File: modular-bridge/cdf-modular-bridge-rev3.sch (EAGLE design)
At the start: 25 parts, among them Q1 Ixgh48n60a3, Q2 Ixgh48n60a3, T1 PULSE-P0584NL

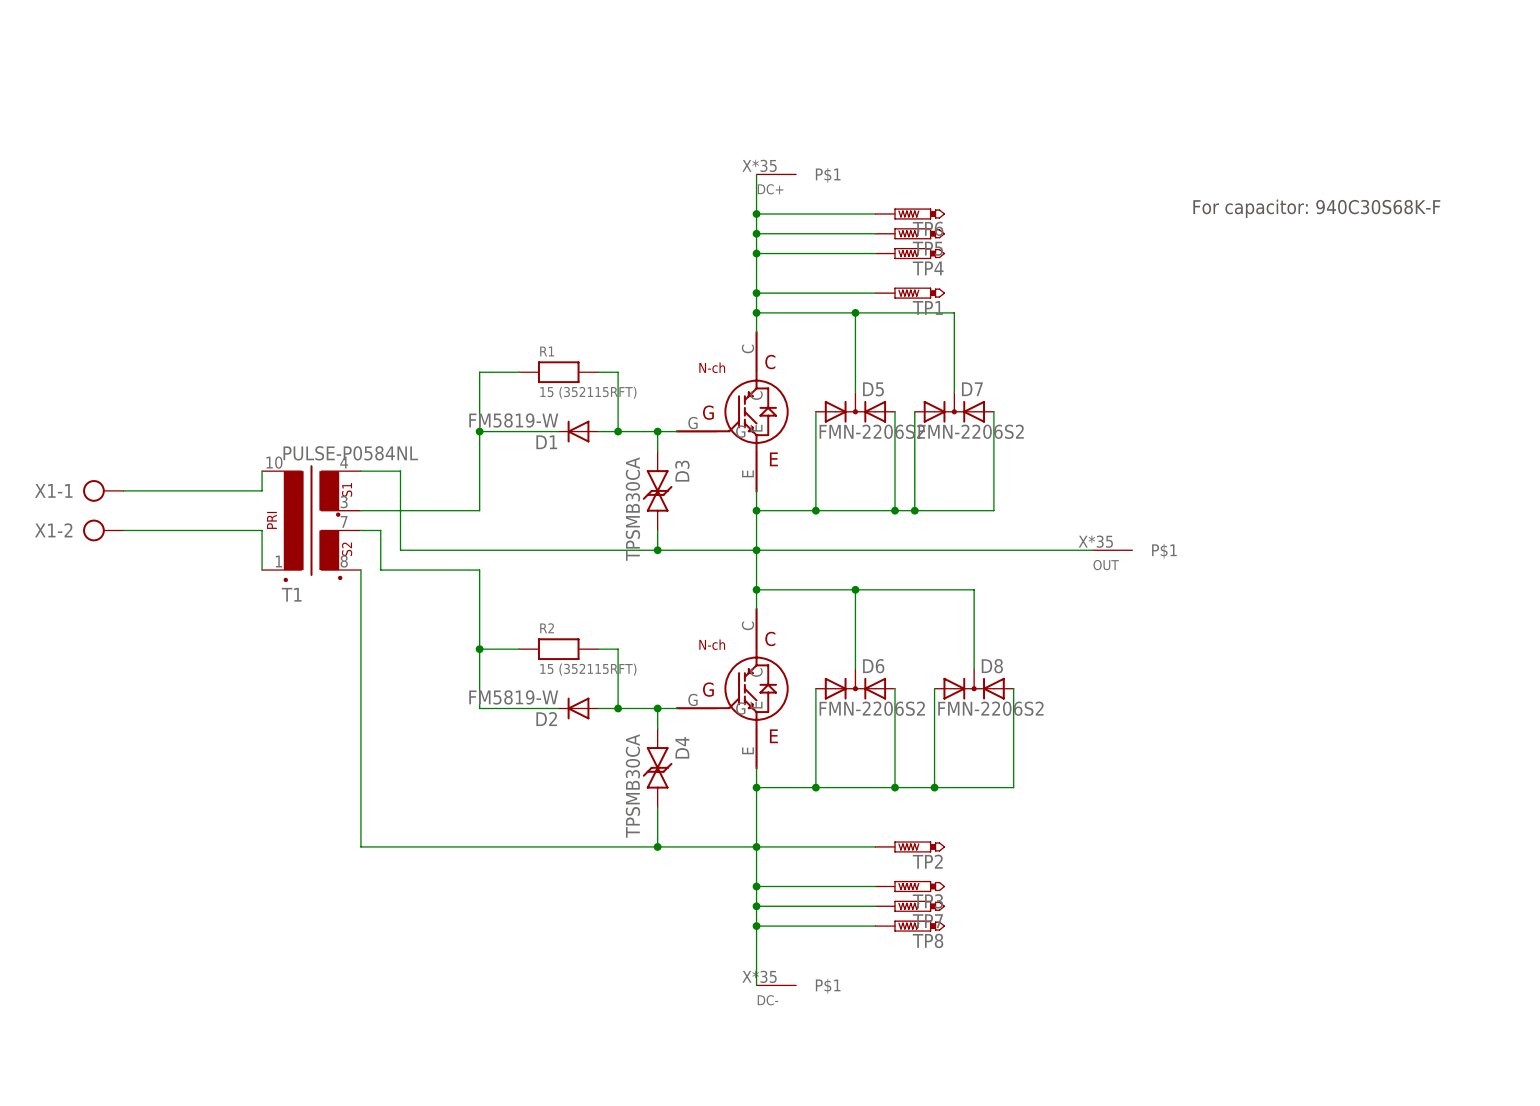
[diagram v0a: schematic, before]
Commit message: add vias
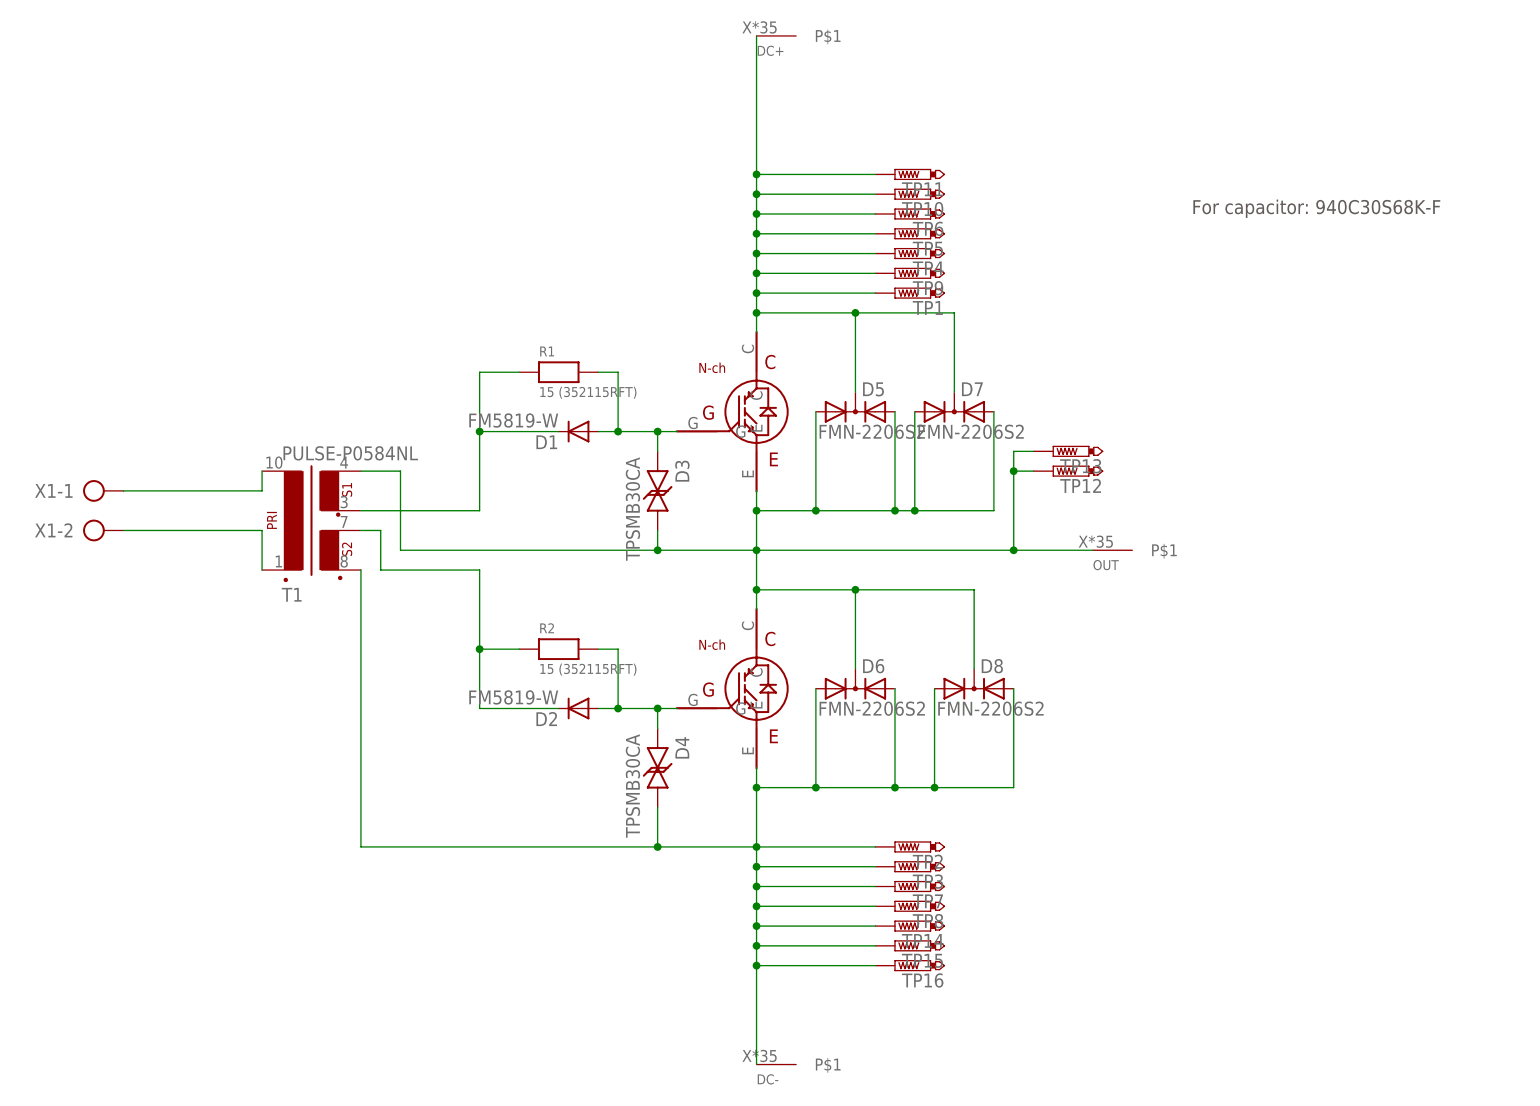
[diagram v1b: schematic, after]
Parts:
- added TP10, TP11, TP12, TP13, TP14, TP15, TP16, TP9: PTR1PAD1-17, testpad:PTR1PAD1-17
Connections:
- net DC+: now also TP10.TP, TP11.TP, TP9.TP
- net DC-: now also TP14.TP, TP15.TP, TP16.TP
- net OUT: now also TP12.TP, TP13.TP
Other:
- moved on the sheet: DC+, DC-, TP3, TP7, TP8
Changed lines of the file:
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@@
 <part name="TP7" library="testpad" deviceset="PTR1" device="PAD1-17"/>
 <part name="TP8" library="testpad" deviceset="PTR1" device="PAD1-17"/>
+<part name="TP9" library="testpad" deviceset="PTR1" device="PAD1-17"/>
+<part name="TP10" library="testpad" deviceset="PTR1" device="PAD1-17"/>
+<part name="TP11" library="testpad" deviceset="PTR1" device="PAD1-17"/>
+<part name="TP14" library="testpad" deviceset="PTR1" device="PAD1-17"/>
+<part name="TP15" library="testpad" deviceset="PTR1" device="PAD1-17"/>
+<part name="TP16" library="testpad" deviceset="PTR1" device="PAD1-17"/>
+<part name="TP12" library="testpad" deviceset="PTR1" device="PAD1-17"/>
+<part name="TP13" library="testpad" deviceset="PTR1" device="PAD1-17"/>
 </parts>
 <sheets>
@@
 <instance part="X1" gate="-2" x="-12.7" y="60.96"/>
 <instance part="OUT" gate="G$1" x="119.38" y="58.42"/>
-<instance part="DC+" gate="G$1" x="76.2" y="106.68"/>
-<instance part="DC-" gate="G$1" x="76.2" y="2.54"/>
+<instance part="DC+" gate="G$1" x="76.2" y="124.46"/>
+<instance part="DC-" gate="G$1" x="76.2" y="-7.62"/>
 <instance part="TP1" gate="G$1" x="91.44" y="91.44" rot="R90"/>
 <instance part="TP2" gate="G$1" x="91.44" y="20.32" rot="R90"/>
@@
 <instance part="D6" gate="1" x="86.36" y="40.64"/>
 <instance part="D8" gate="1" x="101.6" y="40.64"/>
-<instance part="TP3" gate="G$1" x="91.44" y="15.24" rot="R90"/>
+<instance part="TP3" gate="G$1" x="91.44" y="17.78" rot="R90"/>
 <instance part="TP4" gate="G$1" x="91.44" y="96.52" rot="R90"/>
 <instance part="TP5" gate="G$1" x="91.44" y="99.06" rot="R90"/>
 <instance part="TP6" gate="G$1" x="91.44" y="101.6" rot="R90"/>
-<instance part="TP7" gate="G$1" x="91.44" y="12.7" rot="R90"/>
-<instance part="TP8" gate="G$1" x="91.44" y="10.16" rot="R90"/>
+<instance part="TP7" gate="G$1" x="91.44" y="15.24" rot="R90"/>
+<instance part="TP8" gate="G$1" x="91.44" y="12.7" rot="R90"/>
+<instance part="TP9" gate="G$1" x="91.44" y="93.98" rot="R90"/>
+<instance part="TP10" gate="G$1" x="91.44" y="104.14" rot="R90"/>
+<instance part="TP11" gate="G$1" x="91.44" y="106.68" rot="R90"/>
+<instance part="TP14" gate="G$1" x="91.44" y="10.16" rot="R90"/>
+<instance part="TP15" gate="G$1" x="91.44" y="7.62" rot="R90"/>
+<instance part="TP16" gate="G$1" x="91.44" y="5.08" rot="R90"/>
+<instance part="TP12" gate="G$1" x="111.76" y="68.58" rot="R90"/>
+<instance part="TP13" gate="G$1" x="111.76" y="71.12" rot="R90"/>
 </instances>
 <busses>
@@
 <junction x="60.96" y="58.42"/>
 <wire x1="73.66" y1="53.34" x2="73.66" y2="58.42" width="0.1524" layer="91"/>
-<wire x1="73.66" y1="58.42" x2="116.84" y2="58.42" width="0.1524" layer="91"/>
+<wire x1="73.66" y1="58.42" x2="106.68" y2="58.42" width="0.1524" layer="91"/>
 <pinref part="OUT" gate="G$1" pin="P$1"/>
+<wire x1="106.68" y1="58.42" x2="116.84" y2="58.42" width="0.1524" layer="91"/>
 <wire x1="60.96" y1="58.42" x2="27.94" y2="58.42" width="0.1524" layer="91"/>
 <wire x1="27.94" y1="58.42" x2="27.94" y2="68.58" width="0.1524" layer="91"/>
@@
 <junction x="81.28" y="63.5"/>
 <junction x="73.66" y="63.5"/>
+<pinref part="TP13" gate="G$1" pin="TP"/>
+<wire x1="109.22" y1="71.12" x2="106.68" y2="71.12" width="0.1524" layer="91"/>
+<wire x1="106.68" y1="71.12" x2="106.68" y2="68.58" width="0.1524" layer="91"/>
+<pinref part="TP12" gate="G$1" pin="TP"/>
+<wire x1="106.68" y1="68.58" x2="106.68" y2="58.42" width="0.1524" layer="91"/>
+<wire x1="109.22" y1="68.58" x2="106.68" y2="68.58" width="0.1524" layer="91"/>
+<junction x="106.68" y="68.58"/>
+<junction x="106.68" y="58.42"/>
 </segment>
 </net>
@@
 <wire x1="60.96" y1="20.32" x2="22.86" y2="20.32" width="0.1524" layer="91"/>
 <junction x="60.96" y="20.32"/>
-<wire x1="73.66" y1="20.32" x2="73.66" y2="15.24" width="0.1524" layer="91"/>
 <junction x="73.66" y="20.32"/>
 <pinref part="DC-" gate="G$1" pin="P$1"/>
+<wire x1="73.66" y1="20.32" x2="73.66" y2="17.78" width="0.1524" layer="91"/>
+<wire x1="73.66" y1="17.78" x2="73.66" y2="15.24" width="0.1524" layer="91"/>
 <wire x1="73.66" y1="15.24" x2="73.66" y2="12.7" width="0.1524" layer="91"/>
 <wire x1="73.66" y1="12.7" x2="73.66" y2="10.16" width="0.1524" layer="91"/>
-<wire x1="73.66" y1="10.16" x2="73.66" y2="2.54" width="0.1524" layer="91"/>
+<wire x1="73.66" y1="10.16" x2="73.66" y2="7.62" width="0.1524" layer="91"/>
+<wire x1="73.66" y1="7.62" x2="73.66" y2="5.08" width="0.1524" layer="91"/>
+<wire x1="73.66" y1="5.08" x2="73.66" y2="-7.62" width="0.1524" layer="91"/>
 <wire x1="88.9" y1="20.32" x2="73.66" y2="20.32" width="0.1524" layer="91"/>
 <pinref part="T1" gate="G$1" pin="SEC2_POS"/>
@@
 <junction x="96.52" y="27.94"/>
 <pinref part="TP3" gate="G$1" pin="TP"/>
+<wire x1="88.9" y1="17.78" x2="73.66" y2="17.78" width="0.1524" layer="91"/>
+<junction x="73.66" y="17.78"/>
+<pinref part="TP7" gate="G$1" pin="TP"/>
 <wire x1="88.9" y1="15.24" x2="73.66" y2="15.24" width="0.1524" layer="91"/>
+<pinref part="TP8" gate="G$1" pin="TP"/>
+<wire x1="73.66" y1="12.7" x2="88.9" y2="12.7" width="0.1524" layer="91"/>
+<junction x="73.66" y="12.7"/>
 <junction x="73.66" y="15.24"/>
-<pinref part="TP7" gate="G$1" pin="TP"/>
-<wire x1="88.9" y1="12.7" x2="73.66" y2="12.7" width="0.1524" layer="91"/>
-<pinref part="TP8" gate="G$1" pin="TP"/>
-<wire x1="73.66" y1="10.16" x2="88.9" y2="10.16" width="0.1524" layer="91"/>
+<pinref part="TP16" gate="G$1" pin="TP"/>
+<wire x1="88.9" y1="5.08" x2="73.66" y2="5.08" width="0.1524" layer="91"/>
+<pinref part="TP15" gate="G$1" pin="TP"/>
+<wire x1="88.9" y1="7.62" x2="73.66" y2="7.62" width="0.1524" layer="91"/>
+<pinref part="TP14" gate="G$1" pin="TP"/>
+<wire x1="88.9" y1="10.16" x2="73.66" y2="10.16" width="0.1524" layer="91"/>
 <junction x="73.66" y="10.16"/>
-<junction x="73.66" y="12.7"/>
+<junction x="73.66" y="7.62"/>
+<junction x="73.66" y="5.08"/>
 </segment>
 </net>
@@
 <pinref part="DC+" gate="G$1" pin="P$1"/>
 <wire x1="73.66" y1="88.9" x2="73.66" y2="91.44" width="0.1524" layer="91"/>
-<wire x1="73.66" y1="91.44" x2="73.66" y2="96.52" width="0.1524" layer="91"/>
+<wire x1="73.66" y1="91.44" x2="73.66" y2="93.98" width="0.1524" layer="91"/>
+<wire x1="73.66" y1="93.98" x2="73.66" y2="96.52" width="0.1524" layer="91"/>
 <wire x1="73.66" y1="96.52" x2="73.66" y2="99.06" width="0.1524" layer="91"/>
 <wire x1="73.66" y1="99.06" x2="73.66" y2="101.6" width="0.1524" layer="91"/>
-<wire x1="73.66" y1="101.6" x2="73.66" y2="106.68" width="0.1524" layer="91"/>
+<wire x1="73.66" y1="101.6" x2="73.66" y2="104.14" width="0.1524" layer="91"/>
+<wire x1="73.66" y1="104.14" x2="73.66" y2="106.68" width="0.1524" layer="91"/>
+<wire x1="73.66" y1="106.68" x2="73.66" y2="124.46" width="0.1524" layer="91"/>
 <wire x1="88.9" y1="91.44" x2="73.66" y2="91.44" width="0.1524" layer="91"/>
 <junction x="73.66" y="91.44"/>
@@
 <junction x="73.66" y="101.6"/>
 <junction x="73.66" y="99.06"/>
-</segment>
-</net>
+<pinref part="TP9" gate="G$1" pin="TP"/>
+<wire x1="88.9" y1="93.98" x2="73.66" y2="93.98" width="0.1524" layer="91"/>
+<pinref part="TP10" gate="G$1" pin="TP"/>
+<wire x1="88.9" y1="104.14" x2="73.66" y2="104.14" width="0.1524" layer="91"/>
+<pinref part="TP11" gate="G$1" pin="TP"/>
+<wire x1="88.9" y1="106.68" x2="73.66" y2="106.68" width="0.1524" layer="91"/>
+<junction x="73.66" y="106.68"/>
+<junction x="73.66" y="104.14"/>
+<junction x="73.66" y="93.98"/>
+</segment>
+</net>
